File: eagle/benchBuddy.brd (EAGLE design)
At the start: 152.1 x 76.2 mm, 99 parts, among them IC2 TLC274D, IC3 LM334Z, IC4 LM324D, IC5 LM324D, J1 12V_DC, J4 GND, J5 3.3V, J6 5V, J7 12V, J8 GND, J9 0-10V, Q1 600mA/40V, SW4 EG2362, U1 LP2983AIM5-1.0/NOPB, U2 LP2985-10DBVR, U3 3V3REG

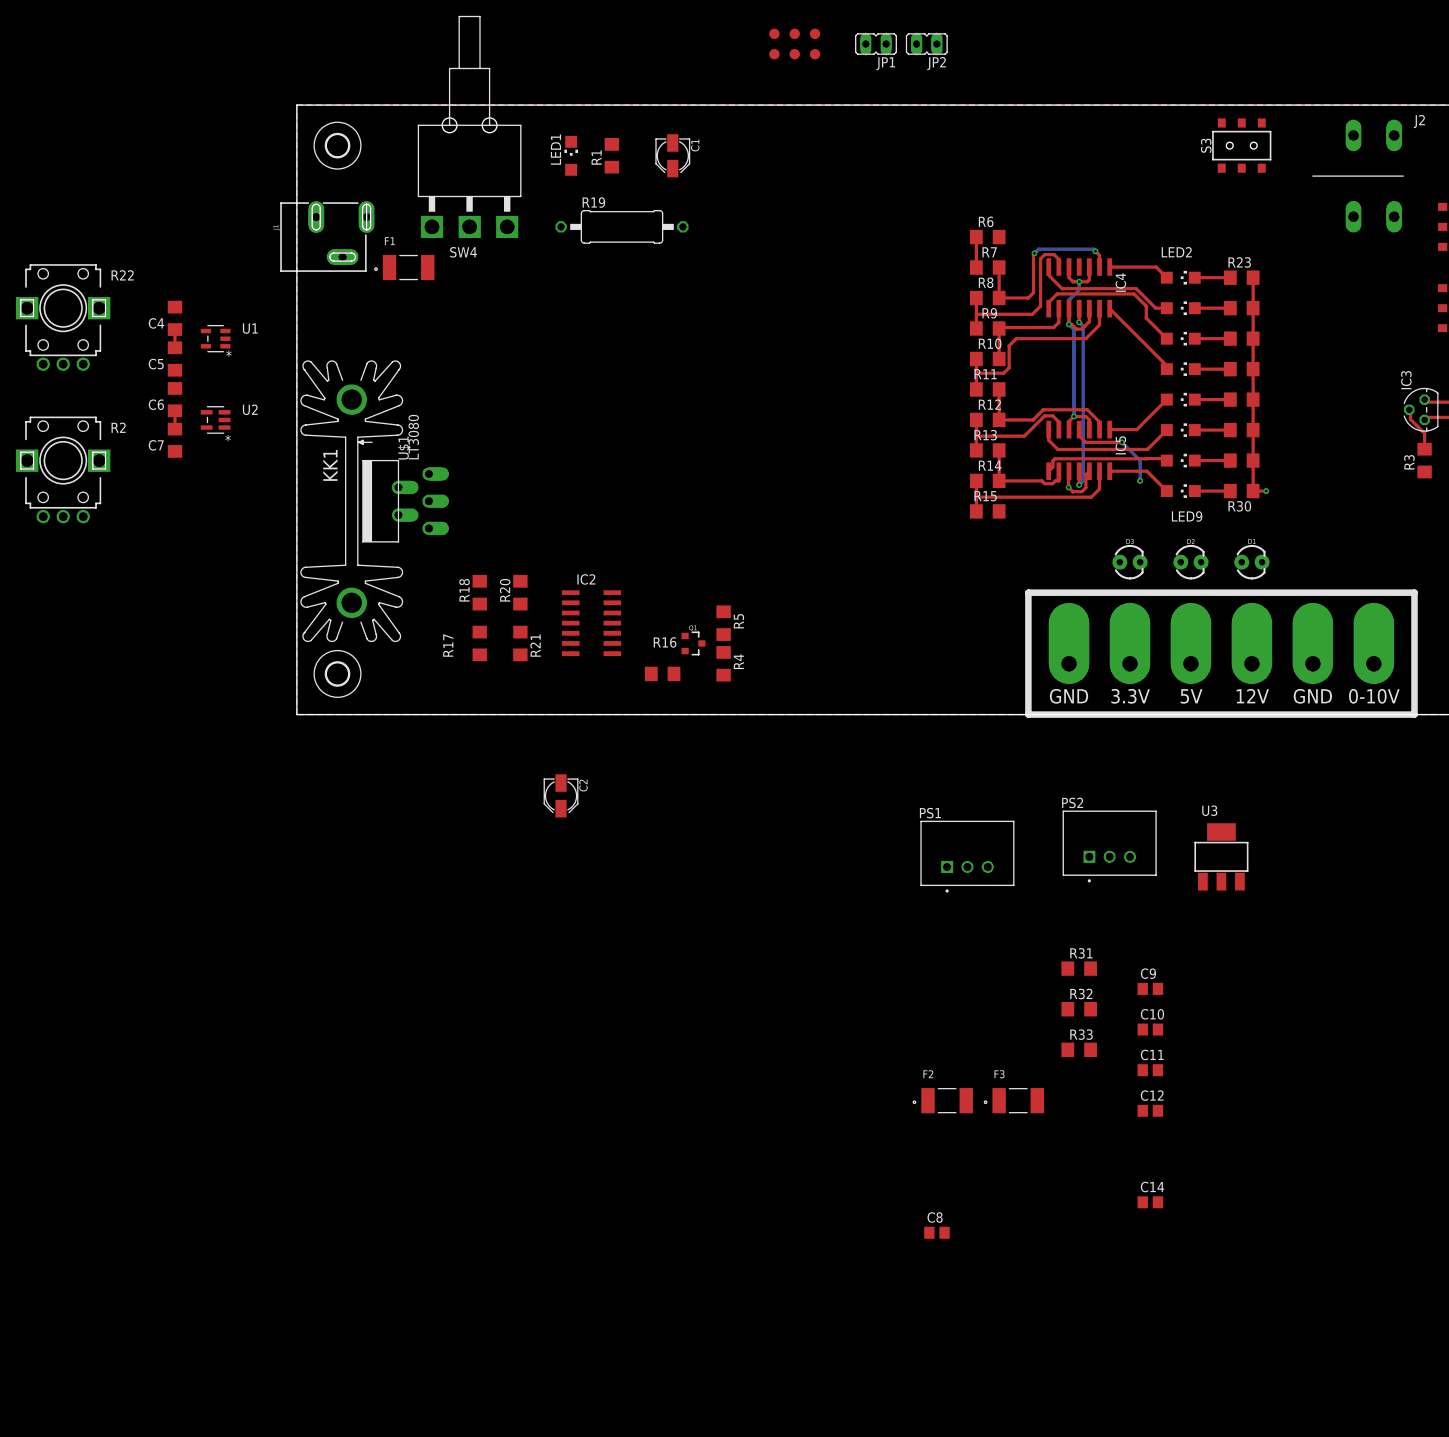
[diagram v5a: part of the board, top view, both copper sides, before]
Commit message: Added mini heatsinks for T220 Packages. Also more work on layout
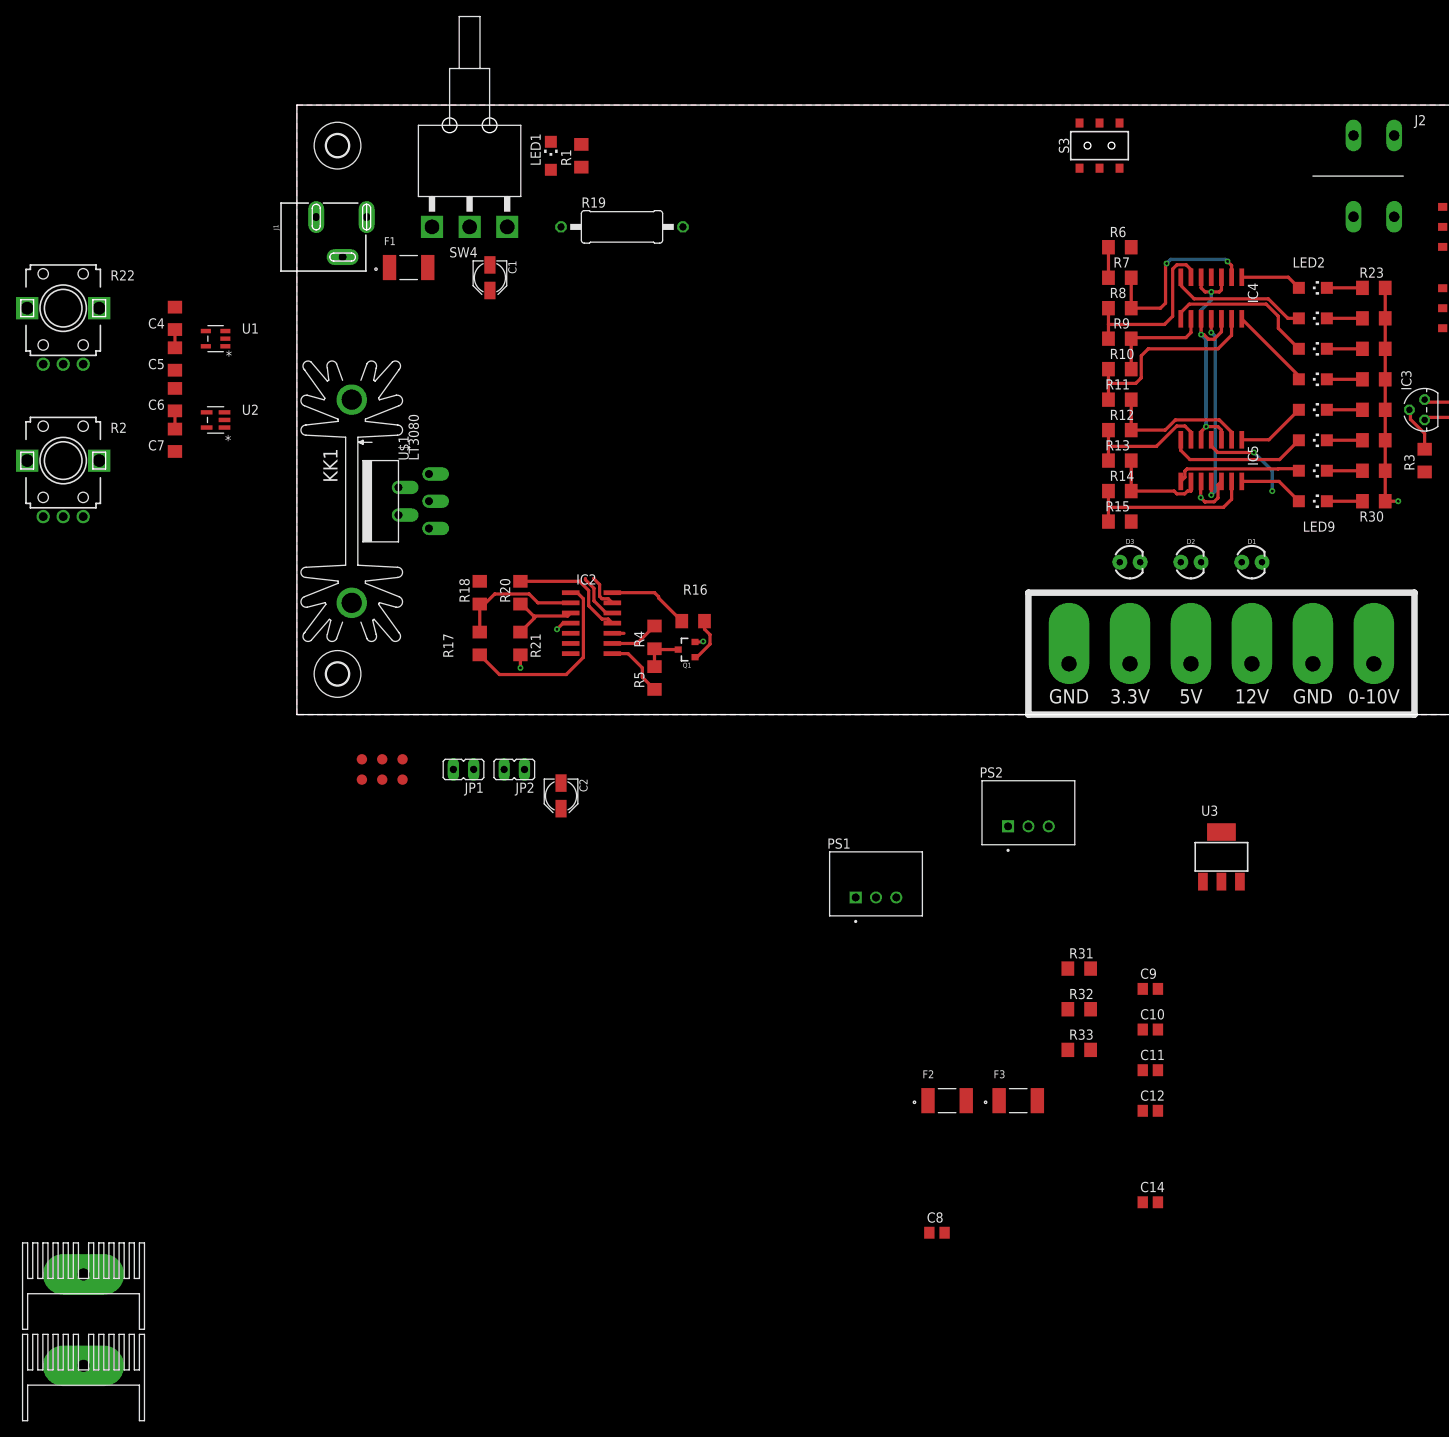
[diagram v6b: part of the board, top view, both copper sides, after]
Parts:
- added U$2, U$3: HEATSINK_MINI, lab07lib:HEATSINK_MINI
- moved JP1 104.3 mm to (20.8, -6.86)
- moved JP2 104.3 mm to (27.2, -6.86)
- moved TP1 104.3 mm to (8.13, -8.13)
- moved TP2 104.3 mm to (8.13, -5.59)
- moved TP3 104.3 mm to (10.7, -8.13)
- moved TP4 104.3 mm to (10.7, -5.59)
- moved TP5 104.3 mm to (13.2, -8.13)
- moved TP6 104.3 mm to (13.2, -5.59)
- moved C1 27.5 mm to (24.1, 54.6)
- moved S3 17.8 mm to (100.3, 71.1)
- moved LED2 16.6 mm to (127.0, 53.3)
- moved LED3 16.6 mm to (127.0, 49.5)
- moved LED4 16.6 mm to (127.0, 45.7)
- moved LED5 16.6 mm to (127.0, 41.9)
- moved LED6 16.6 mm to (127.0, 38.1)
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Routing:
- net I_OUT: track 0.00 -> 30.3 mm
- net N$18: track 0.00 -> 15.4 mm
- net VIN: track 12.2 -> 27.0 mm
- net N$21: track 0.00 -> 10.2 mm
- net N$17: track 0.00 -> 9.86 mm
- net V_OUT: track 0.00 -> 7.81 mm
- net N$6: track 0.00 -> 6.18 mm
- net N$23: track 0.00 -> 5.71 mm
- net N$5: track 0.00 -> 5.24 mm
- net GND: track 65.1 -> 69.8 mm, vias 3 -> 6
- net I_SET: track 0.00 -> 4.47 mm
- net V_SET: track 0.00 -> 1.46 mm

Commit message: Board mostly routed! Added heatsink 3.3V version
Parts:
- U3: value 3V3REG -> 3V3REG-HEATSINK; device PowerManagementParts:SOT223 -> lab07lib:SOT223-HS
- moved JP1 227.7 mm to (206.5, 125.0)
- moved JP2 227.7 mm to (212.9, 125.0)
- moved TP3 227.7 mm to (196.3, 123.7)
- moved TP4 227.7 mm to (196.3, 126.2)
- moved TP5 227.7 mm to (198.9, 123.7)
- moved TP6 227.7 mm to (198.9, 126.2)
- moved TP1 227.7 mm to (193.8, 123.7)
- moved TP2 227.7 mm to (193.8, 126.2)
- moved U$2 114.1 mm to (53.3, 8.89), turned to 270 degrees
- moved U$3 111.0 mm to (34.3, 8.89), turned to 90 degrees
- moved C14 109.6 mm to (44.5, 29.2), turned to 180 degrees
- moved S2 98.3 mm to (48.3, 71.1), turned to 0 degrees
- moved C12 86.5 mm to (58.9, 22.6), turned to 90 degrees
- moved S1 85.0 mm to (63.5, 71.1), turned to 0 degrees
- moved F3 84.6 mm to (40.6, 20.3), turned to 270 degrees
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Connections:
- net I_SET_MICRO: now also J3.4; no longer J3.3
- net VCC: now also J3.3; no longer J3.4
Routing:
- net VCC: track 8.02 -> 222.2 mm, vias 0 -> 4
- net 10VOLTS: track 0.00 -> 136.1 mm, vias 0 -> 5
- net I_OUT: track 30.3 -> 139.6 mm, vias 0 -> 5
- net GND: track 69.8 -> 162.0 mm, vias 6 -> 15
- net 5V: track 0.00 -> 85.9 mm, vias 0 -> 1
- net V_SET: track 1.46 -> 70.0 mm, vias 0 -> 6
- net 1VOLT: track 0.00 -> 58.7 mm, vias 0 -> 1
- net V_SET_POT: track 0.00 -> 57.5 mm, vias 0 -> 6
- net I_SET: track 4.47 -> 57.9 mm, vias 0 -> 2
- net N$6: track 6.18 -> 54.7 mm, vias 0 -> 2
- net I_SET_MICRO: track 0.00 -> 47.9 mm
- net V_SET_MICRO: track 0.00 -> 47.2 mm
- net DISPLAY: track 42.5 -> 88.4 mm, vias 4 -> 8
- net VIN: track 27.0 -> 65.0 mm, vias 2 -> 4
- net VOLT_RANGE: track 0.00 -> 36.7 mm, vias 0 -> 2
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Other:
- board size 152.1 x 76.2 mm -> 122.9 x 76.2 mm

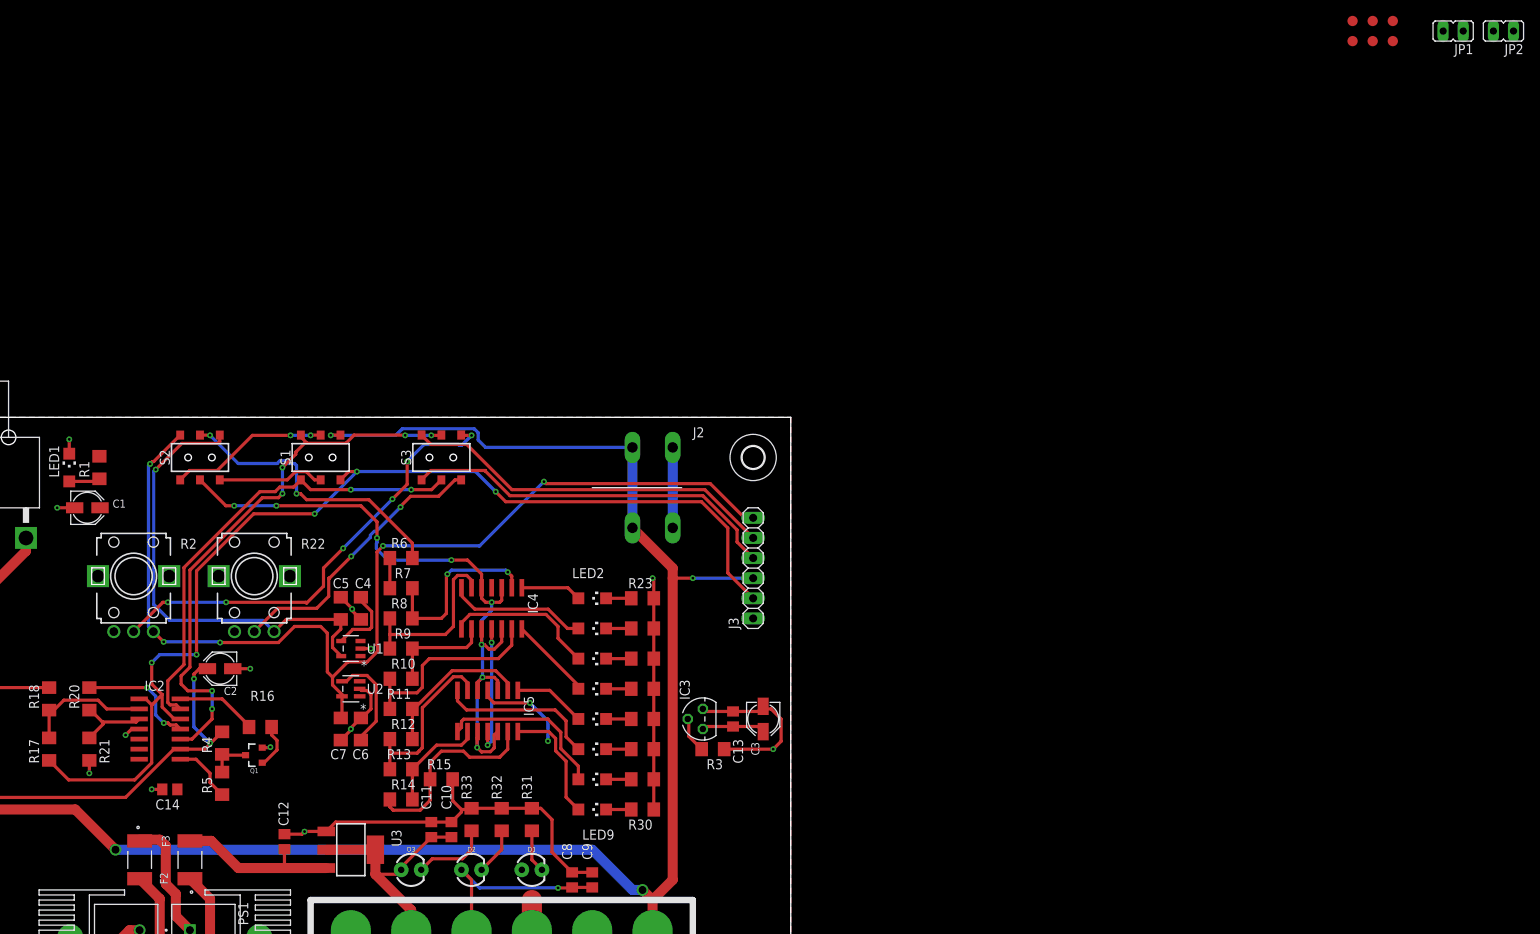
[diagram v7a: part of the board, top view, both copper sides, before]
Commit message: Board fully routed. Added test header
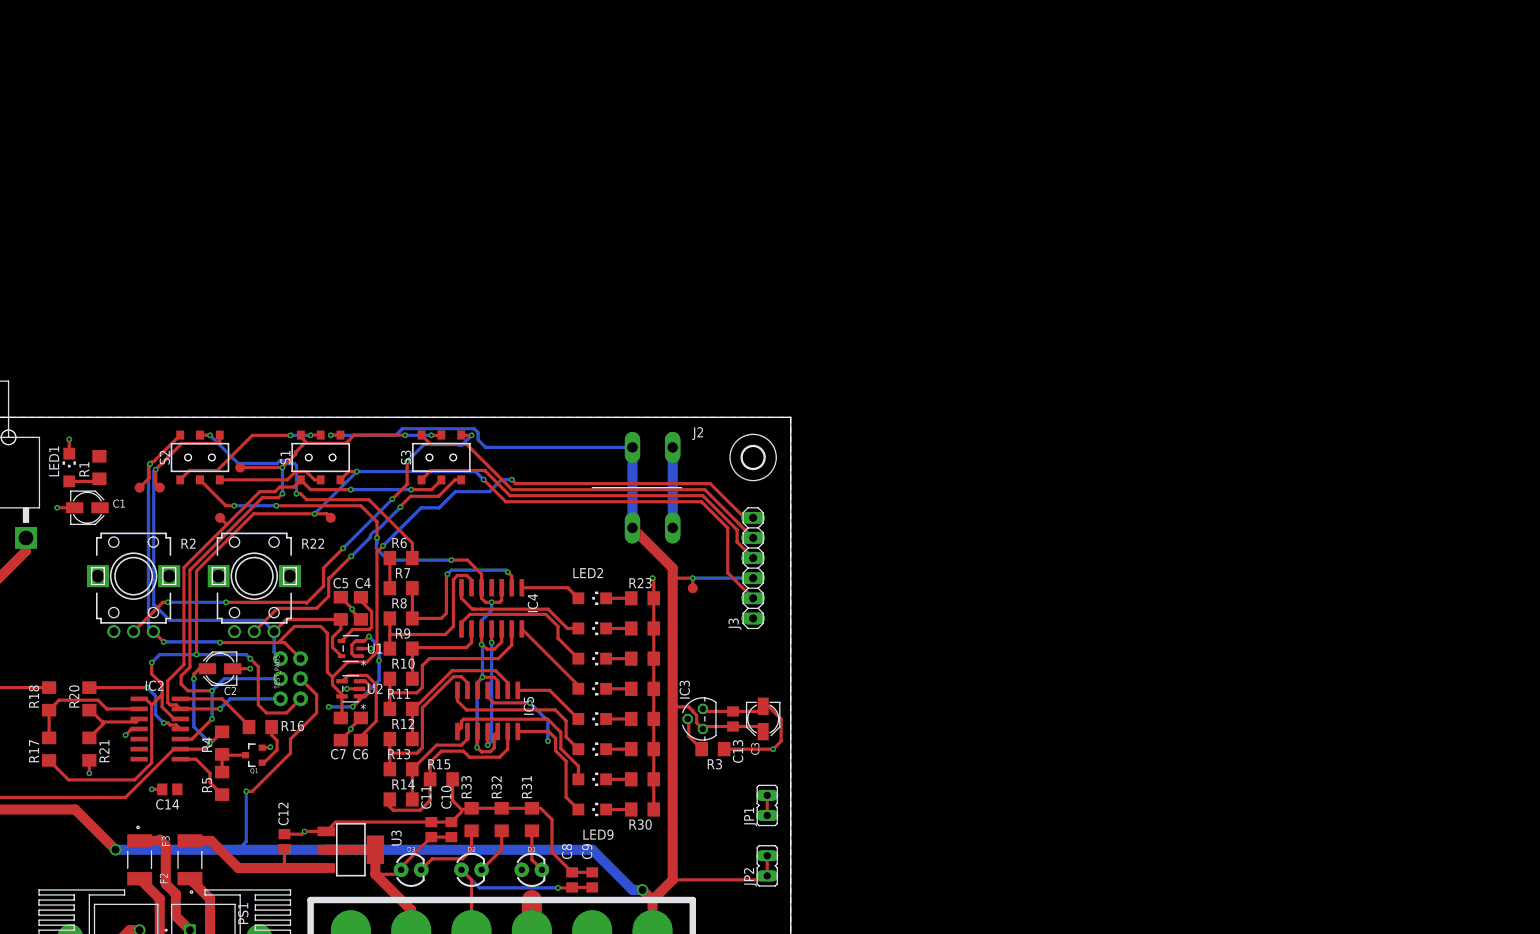
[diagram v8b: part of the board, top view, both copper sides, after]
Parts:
- removed TP1, TP2, TP3, TP4, TP5, TP6: TPTP13R, testpad:TP13R
- added TEST_PADS: (no value), SparkFun-Connectors:2X3-NS
- added TP_10VOLTS, TP_1VOLT, TP_IOUT, TP_ISET, TP_VCC, TP_VSET: TPB1,27, testpad:B1,27
- U1: value LP2983AIM5-1.0/NOPB -> LP2983AIM5-1.0/NOPBMF05A-L; device lab07lib:MF05A -> lab07lib:MF05A-L
- moved JP2 140.5 mm to (119.9, 19.6), turned to 0 degrees
- moved JP1 130.6 mm to (119.9, 27.2), turned to 0 degrees
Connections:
- net 10VOLTS: now also TEST_PADS.5, TP_10VOLTS.TP; no longer TP6.TP
- net 1VOLT: now also TEST_PADS.6, TP_1VOLT.TP; no longer TP5.TP
- net I_OUT: now also TEST_PADS.1, TP_IOUT.TP; no longer TP4.TP
- net I_SET: now also TEST_PADS.2, TP_ISET.TP; no longer TP3.TP
- net VCC: now also TEST_PADS.3, TP_VCC.TP; no longer TP2.TP
- net V_SET: now also TEST_PADS.4, TP_VSET.TP; no longer TP1.TP
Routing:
- net VCC: track 222.2 -> 270.7 mm, vias 4 -> 5
- net VIN: track 65.0 -> 89.0 mm, vias 4 -> 8
- net I_OUT: track 139.6 -> 161.6 mm, vias 5 -> 6
- net V_SET: track 70.0 -> 84.6 mm
- net I_SET: track 57.9 -> 72.3 mm, vias 2 -> 3
- net 1VOLT: track 58.7 -> 65.0 mm
- net 10VOLTS: track 136.1 -> 142.2 mm
- net N$45: track 16.4 -> 17.7 mm
- net GND: track 162.0 -> 161.0 mm, vias 15 -> 16
